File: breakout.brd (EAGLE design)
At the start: 25.4 x 32.4 mm, 26 parts, among them IC2 REG1117, Q1 12Mhz, U1 LM358DR

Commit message: adding some dimentions
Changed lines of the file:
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@@
 <grid distance="0.003125" unitdist="inch" unit="inch" style="lines" multiple="1" display="no" altdistance="0.025" altunitdist="inch" altunit="inch"/>
 <layers>
-<layer number="1" name="Top" color="4" fill="1" visible="no" active="yes"/>
+<layer number="1" name="Top" color="4" fill="1" visible="yes" active="yes"/>
 <layer number="2" name="Route2" color="1" fill="3" visible="yes" active="yes"/>
 <layer number="3" name="Route3" color="4" fill="3" visible="no" active="yes"/>
@@
 <plain>
 <wire x1="0" y1="0" x2="25.3875" y2="0" width="0" layer="20"/>
-<wire x1="25.3875" y1="0" x2="25.3875" y2="32.375" width="0" layer="20"/>
-<wire x1="25.3875" y1="32.375" x2="0" y2="32.375" width="0" layer="20"/>
-<wire x1="0" y1="32.375" x2="0" y2="0" width="0" layer="20"/>
+<wire x1="25.3875" y1="0" x2="25.4" y2="32.385" width="0" layer="20"/>
+<wire x1="25.4" y1="32.385" x2="0" y2="32.385" width="0" layer="20"/>
+<wire x1="0" y1="32.385" x2="0" y2="0" width="0" layer="20"/>
 <text x="22.304375" y="9.2075" size="1.4224" layer="26" rot="MR0">git.io/vwtq7</text>
 <text x="22.304375" y="6.82625" size="1.4224" layer="26" rot="MR0">@matthewbaggett</text>
+<dimension x1="1.27" y1="30.1625" x2="24.13" y2="30.1625" x3="12.7" y3="38.25875" textsize="5.08" layer="150"/>
+<dimension x1="0" y1="0" x2="25.4" y2="0" x3="12.7" y3="-11.509375" textsize="5.08" layer="150"/>
+<dimension x1="25.3875" y1="0" x2="25.4" y2="32.385" x3="34.443565625" y3="16.18900625" textsize="5.08" layer="150"/>
+<dimension x1="1.27" y1="30.1625" x2="1.27" y2="27.6225" x3="-5.08" y3="28.8925" textsize="5.08" layer="150"/>
+<dimension x1="17.859375" y1="39.0525" x2="17.859375" y2="-1.42875" x3="46.273321875" y3="18.811875" textsize="5.08" layer="150"/>
 </plain>
 <attributes>

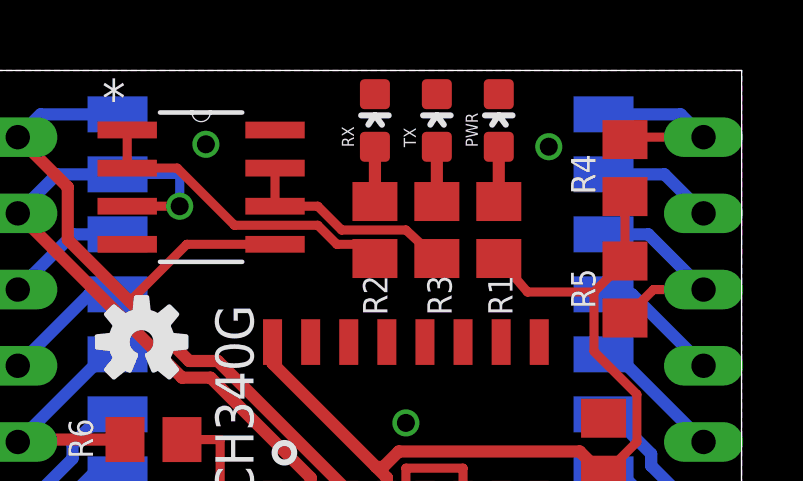
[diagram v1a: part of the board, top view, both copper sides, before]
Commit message: Missing line for the LM358DR
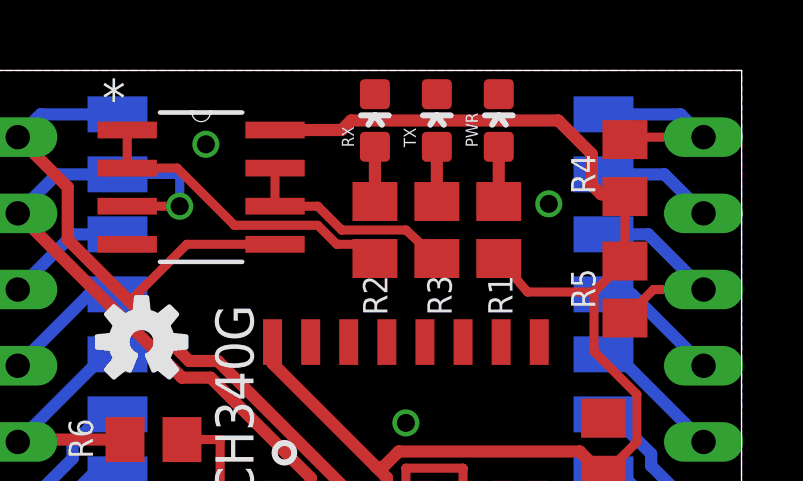
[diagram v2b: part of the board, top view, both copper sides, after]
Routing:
- net 3.3V: track 67.4 -> 80.9 mm
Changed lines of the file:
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@@
 <wire x1="8.016875" y1="20.081875" x2="8.016875" y2="16.8275" width="0.3048" layer="1"/>
 <contactref element="U1" pad="8"/>
-<wire x1="9.763125" y1="23.3325" x2="9.845675" y2="30.400625" width="0" layer="19" extent="1-1"/>
+<wire x1="9.845675" y1="30.400625" x2="12.065" y2="30.400625" width="0.4064" layer="1"/>
+<wire x1="12.065" y1="30.400625" x2="12.3825" y2="30.718125" width="0.4064" layer="1"/>
+<wire x1="12.3825" y1="30.718125" x2="19.288125" y2="30.718125" width="0.4064" layer="1"/>
+<wire x1="19.288125" y1="30.718125" x2="20.399375" y2="29.606875" width="0.4064" layer="1"/>
+<wire x1="20.399375" y1="29.606875" x2="20.399375" y2="28.575" width="0.4064" layer="1"/>
+<wire x1="20.399375" y1="28.575" x2="20.716875" y2="28.2575" width="0.4064" layer="1"/>
+<wire x1="20.716875" y1="28.2575" x2="21.43375" y2="28.2575" width="0.4064" layer="1"/>
+<wire x1="21.43375" y1="28.2575" x2="21.510625" y2="28.180625" width="0.4064" layer="1"/>
 </signal>
 <signal name="GPIO13">
@@
 <via x="7.9375" y="10.795" extent="1-16" drill="0.6"/>
 <via x="14.208125" y="20.6375" extent="1-16" drill="0.6"/>
-<via x="18.970625" y="29.845" extent="1-16" drill="0.6"/>
+<via x="18.970625" y="27.94" extent="1-16" drill="0.6"/>
 <contactref element="U1" pad="4"/>
 <contactref element="RX" pad="C"/>
